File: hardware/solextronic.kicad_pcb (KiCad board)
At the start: 2 copper layers, 100 x 80 mm, 39 parts, among them J1 DB25, P1 CONN_4, P2 CONN_4, P3 CONN_2, Q1 IRL540, Q2 BC237, U1 25LC256, U2 LM324, U3 4N25, U4 4N25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

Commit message: HW - Renommage des signaux et mise à jour carte de test
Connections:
- net /PMH renamed /Motor
- net /Pressure renamed /MAP
- net /PressureAdc renamed /MAPAdc
- net /Tair renamed /IAT
- net /Throttle renamed /TPS
- net /ThrottleAdc renamed /TPSAdc
- net /Tmotor renamed /CLT
- net /TmotorAdc renamed /CLTAdc
- net /TopPMH renamed /TopMotor
- U2 pad 6: /TairAdc -> /IATAdc
- U2 pad 7: /TairAdc -> /IATAdc
- U6 pad 25: /TairAdc -> (no net)
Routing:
- net /TairAdc: track 19.7 -> 0.00 mm
- net /IATAdc: track 0.00 -> 19.7 mm

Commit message: HW - Debut optim carte principale
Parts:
- removed U4: 4N25, DIP-6__300
- added R15: 470, R3, F.Cu at (135.9, 118.1)
- added R16: 470, R3, F.Cu at (135.9, 120.7)
- R11, R7, R8: value 10k -> 4.7k
- U3: value 4N25 -> CNY74-2; footprint DIP-6__300 -> DIP-8__300
- moved R7 27.3 mm to (177.2, 106.0)
- moved R8 23.1 mm to (174.6, 108.6)
- moved U3 1.27 mm to (151.8, 134.6)
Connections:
- C2 pad 1: N-000001 -> N-0000017
- C3 pad 1: N-000006 -> N-000002
- C4 pad 1: N-0000033 -> N-000004
- C5 pad 1: N-0000036 -> N-0000026
- D1 pad 2: /CLT -> N-0000017
- D2 pad 2: /IAT -> N-000002
- D3 pad 2: /MAP -> N-000004
- D4 pad 2: /TPS -> N-0000026
- R1 pad 2: N-000001 -> N-0000017
- R2 pad 2: N-000006 -> N-000002
- R3 pad 2: N-0000033 -> N-000004
- R4 pad 2: N-0000036 -> N-0000026
- R5 pad 2: N-0000042 (its old number) -> N-0000023
- R6 pad 2: N-0000043 -> N-0000022
- R7 pad 1: +5V -> /Wheel
- R7 pad 2: /Wheel -> +5V
- R8 pad 1: +5V -> /Motor
- R8 pad 2: /Motor -> +5V
- U2 pad 10: N-000001 -> N-0000017
- U2 pad 12: N-0000036 -> N-0000026
- U2 pad 3: N-0000033 -> N-000004
- U2 pad 5: N-000006 -> N-000002
- U3 pad 1: N-0000042 (its old number) -> N-0000022
- U3 pad 3: (no net) -> GND
- U3 pad 4: GND -> N-0000023
- U3 pad 5: /Wheel -> GND
- U3 pad 6: (no net) -> /Wheel
- U6 pad 25: (no net) -> /IATAdc
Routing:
- net GND: track 479.4 -> 416.0 mm
- net /BTN1: track 83.1 -> 36.9 mm
- net /Wheel: track 52.5 -> 6.40 mm, vias 2 -> 0
- net /Motor: track 42.2 -> 0.00 mm, vias 2 -> 0
- net N-000002: track 0.00 -> 35.8 mm
- net N-000004: track 0.00 -> 35.6 mm
- net N-0000017: track 0.00 -> 34.3 mm
- net N-000006: track 32.8 -> 0.00 mm
- net N-0000033: track 30.6 -> 0.00 mm
- net N-000001: track 29.3 -> 0.00 mm
- net N-0000023: track 0.00 -> 25.9 mm
- net N-0000043: track 24.1 -> 0.00 mm
- net N-0000042 (its old number): track 23.8 -> 0.00 mm
- net N-0000022: track 0.00 -> 23.8 mm
- net N-0000026: track 0.00 -> 22.7 mm
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
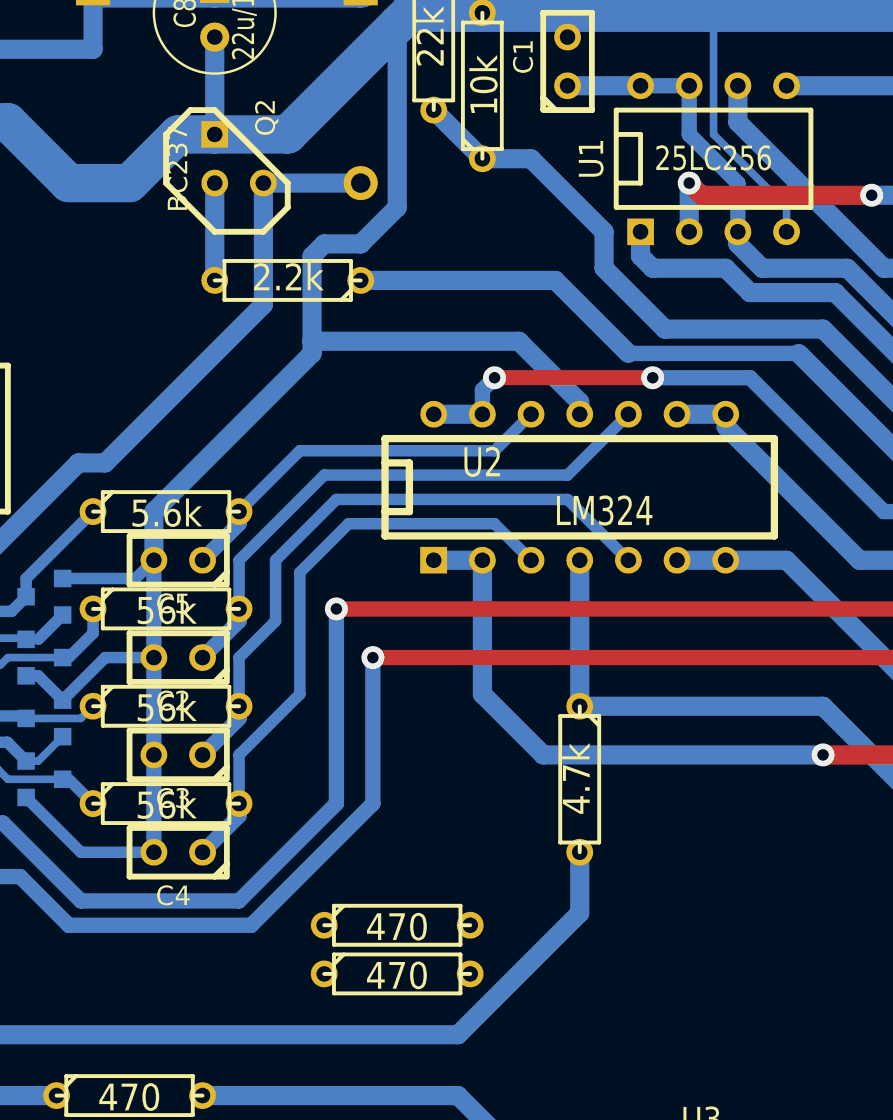
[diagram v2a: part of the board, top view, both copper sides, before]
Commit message: HW - Simplification des entrees
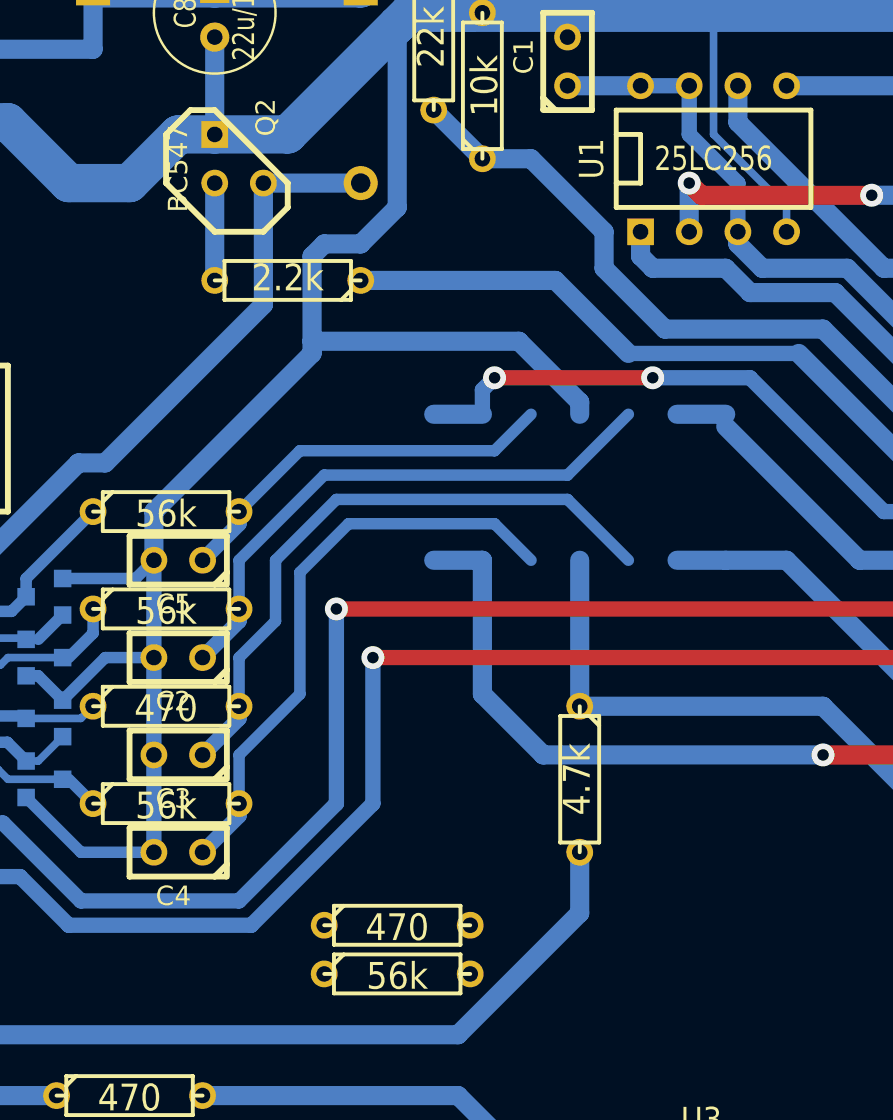
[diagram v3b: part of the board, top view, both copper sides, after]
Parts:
- removed U2: LM324, DIP-14__300
- Q2: value BC237 -> BC547
- R16: value 470 -> 56k
- R2: value 56k -> 470
- R4: value 5.6k -> 56k
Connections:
- C2 pad 1: N-0000017 (its old number) -> /CLTAdc
- C3 pad 1: N-000002 -> /IATAdc
- C4 pad 1: N-000004 -> /MAPAdc
- C5 pad 1: N-0000026 -> /TPSAdc
- D1 pad 2: N-0000017 (its old number) -> /CLTAdc
- D2 pad 2: N-000002 -> /IATAdc
- D3 pad 2: N-000004 -> /MAPAdc
- D4 pad 2: N-0000026 -> /TPSAdc
- R1 pad 2: N-0000017 (its old number) -> /CLTAdc
- R15 pad 1: /CLT -> (no net)
- R16 pad 1: /IAT -> /TPS
- R16 pad 2: +5V -> /TPSAdc
- R2 pad 1: /IAT -> (no net)
- R2 pad 2: N-000002 -> +5V
- R3 pad 1: /MAP -> /IAT
- R3 pad 2: N-000004 -> /IATAdc
- R4 pad 1: /TPS -> /MAP
- R4 pad 2: N-0000026 -> /MAPAdc
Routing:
- net N-000002: track 35.8 -> 0.00 mm
- net N-000004: track 35.6 -> 0.00 mm
- net /IATAdc: track 19.7 -> 54.2 mm
- net N-0000017 (its old number): track 34.3 -> 0.00 mm
- net /CLTAdc: track 20.0 -> 54.4 mm
- net +5V: track 176.4 -> 206.5 mm
- net /MAPAdc: track 37.5 -> 63.2 mm
- net N-0000026: track 22.7 -> 0.00 mm
- net /TPS: track 6.40 -> 1.46 mm
- net /MAP: track 1.48 -> 6.42 mm
- net /TPSAdc: track 33.6 -> 38.4 mm
- net /IAT: track 2.99 -> 2.10 mm

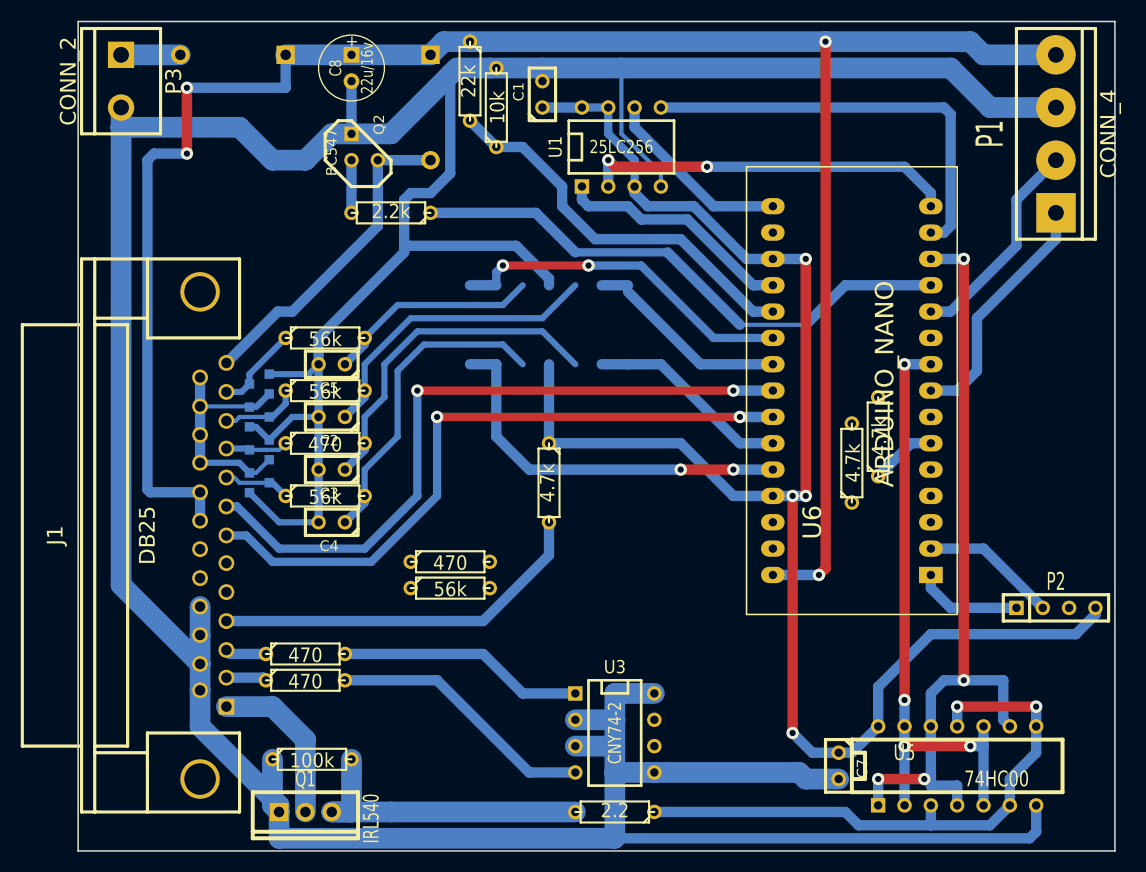
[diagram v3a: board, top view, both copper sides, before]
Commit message: HW - mise a jour du schema principale : simplification pour supprimer le bluetooth
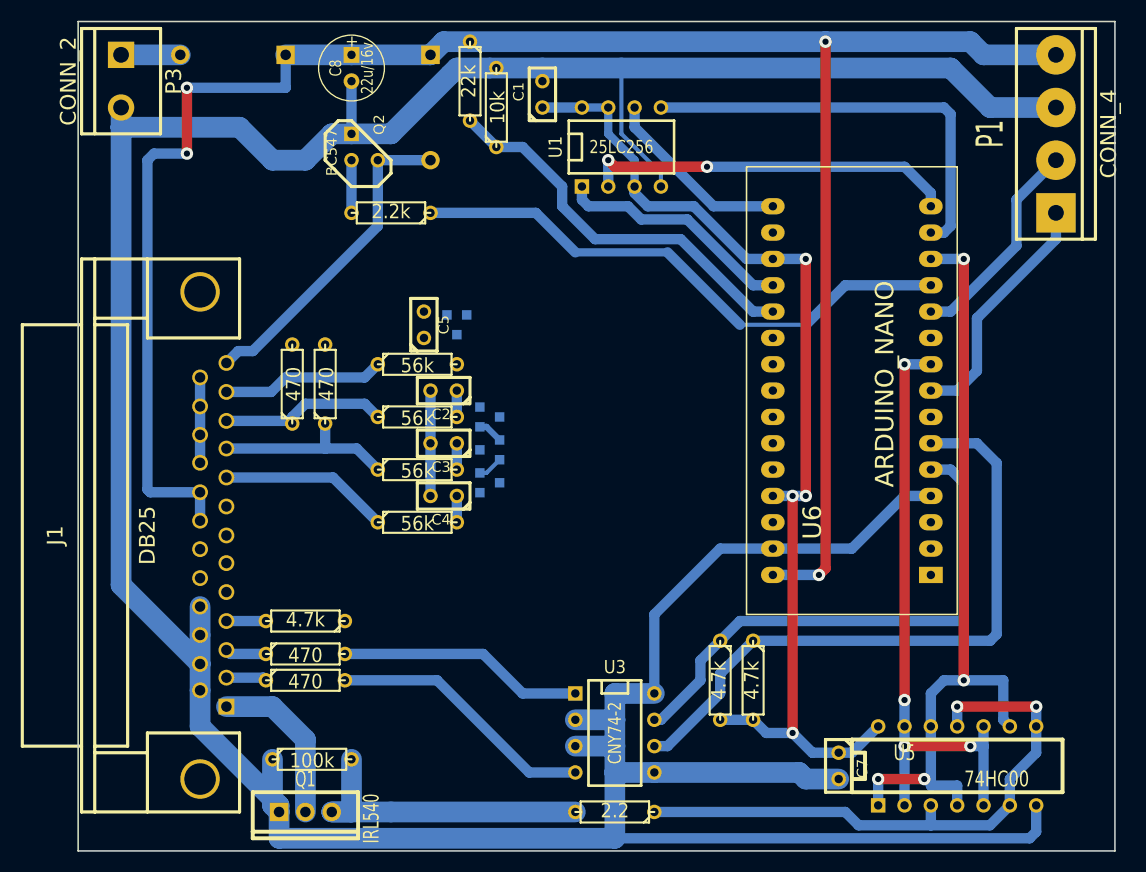
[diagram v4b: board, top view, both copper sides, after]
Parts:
- removed P2: CONN_4, SIL-4
- moved R11 27.0 mm to (121.9, 123.8), turned to 180 degrees
- moved R7 26.4 mm to (165.1, 129.5), turned to 270 degrees
- moved R8 24.5 mm to (161.9, 129.5), turned to 270 degrees
- moved R15 22.9 mm to (120.7, 101.0), turned to 90 degrees
- moved D1 22.2 mm to (139.7, 104.1)
- moved D2 22.2 mm to (139.7, 107.3)
- moved D3 22.2 mm to (139.7, 110.5)
- moved R16 21.8 mm to (132.7, 99.1)
- moved D4 19.9 mm to (136.5, 95.2), turned to 180 degrees
- moved R4 19.9 mm to (132.7, 114.3)
- moved C2 11.1 mm to (135.3, 101.6)
- moved C3 11.1 mm to (135.3, 106.7)
- moved C4 11.1 mm to (135.3, 111.8)
- moved C5 9.67 mm to (133.3, 95.2), turned to 90 degrees
- moved R1 9.25 mm to (132.7, 104.1)
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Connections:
- R15 pad 1: (no net) -> /CLT
- R2 pad 1: (no net) -> /IAT
- U6 pad 1: N-0000018 -> (no net)
- U6 pad 2: N-0000017 (its old number) -> (no net)
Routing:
- net +5V: track 206.5 -> 112.0 mm
- net /FP_DATA: track 66.7 -> 0.00 mm, vias 2 -> 0
- net /FP_CLK: track 64.0 -> 0.00 mm, vias 2 -> 0
- net /MAPAdc: track 63.2 -> 2.54 mm, vias 2 -> 0
- net /Wheel: track 6.40 -> 62.3 mm
- net /Motor: track 0.00 -> 51.9 mm
- net /CLTAdc: track 54.4 -> 2.54 mm
- net /IATAdc: track 54.2 -> 2.54 mm
- net /TPSAdc: track 38.4 -> 0.00 mm, vias 2 -> 0
- net GND: track 416.0 -> 381.0 mm
- net /BTN1: track 36.9 -> 3.81 mm
- net /IAT: track 2.10 -> 17.9 mm
- net /TPS: track 1.46 -> 15.7 mm
- net /CLT: track 2.70 -> 16.4 mm
- net N-0000017 (its old number): track 13.2 -> 0.00 mm
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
